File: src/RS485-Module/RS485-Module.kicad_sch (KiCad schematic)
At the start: 29 parts, among them J1 Jumper_NO, J2 Jumper_NO, J3 Jumper_NO, J4 Jumper_NO, J5 Jumper_NO, J6 Jumper_NO, J7 Jumper_NO, J8 Jumper_NO, P1 5015680807, P2 282837-2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

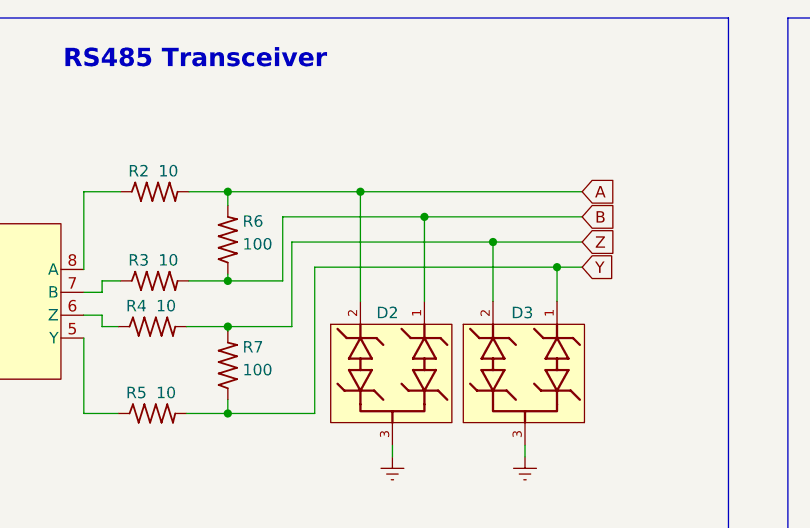
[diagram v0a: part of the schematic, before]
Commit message: placed components in layoyut
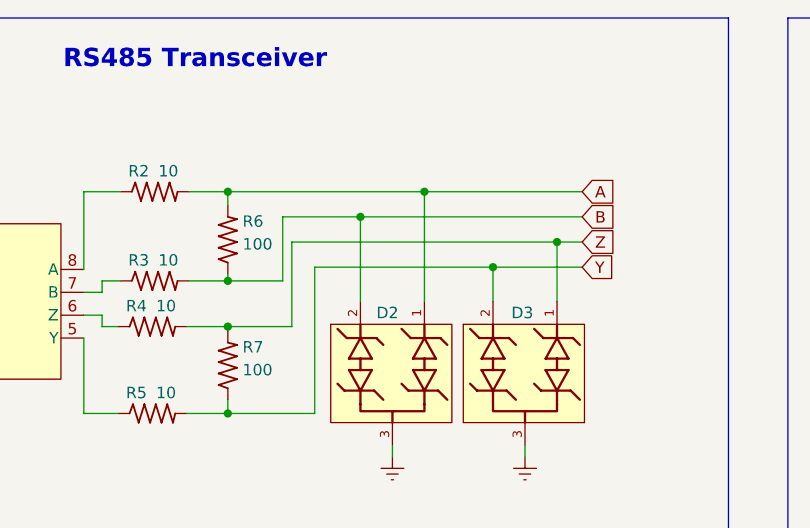
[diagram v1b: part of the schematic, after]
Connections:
- net A: now also D2.1; no longer D2.2
- net B: now also D2.2; no longer D2.1
- net Y: now also D3.2; no longer D3.1
- net Z: now also D3.1; no longer D3.2
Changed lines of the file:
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@@
   (junction (at 166.116 44.958) (diameter 0) (color 0 0 0 0)
   )
-  (junction (at 202.692 53.34) (diameter 0) (color 0 0 0 0)
-  )
   (junction (at 53.594 62.23) (diameter 0) (color 0 0 0 0)
   )
@@
   (junction (at 166.116 59.944) (diameter 0) (color 0 0 0 0)
   )
-  (junction (at 180.848 44.958) (diameter 0) (color 0 0 0 0)
-  )
   (junction (at 108.204 53.34) (diameter 0) (color 0 0 0 0)
   )
+  (junction (at 180.848 47.752) (diameter 0) (color 0 0 0 0)
+  )
   (junction (at 156.972 110.998) (diameter 0) (color 0 0 0 0)
   )
@@
   (junction (at 156.718 122.174) (diameter 0) (color 0 0 0 0)
   )
-  (junction (at 195.58 50.546) (diameter 0) (color 0 0 0 0)
+  (junction (at 187.96 44.958) (diameter 0) (color 0 0 0 0)
+  )
+  (junction (at 195.58 53.34) (diameter 0) (color 0 0 0 0)
   )
   (junction (at 53.594 59.69) (diameter 0) (color 0 0 0 0)
   )
-  (junction (at 187.96 47.752) (diameter 0) (color 0 0 0 0)
+  (junction (at 202.692 50.546) (diameter 0) (color 0 0 0 0)
   )
   (junction (at 166.116 69.596) (diameter 0) (color 0 0 0 0)
@@
     (stroke (width 0) (type default))
   )
+  (wire (pts (xy 202.692 50.546) (xy 202.692 57.15))
+    (stroke (width 0) (type default))
+  )
   (wire (pts (xy 106.68 53.34) (xy 108.204 53.34))
     (stroke (width 0) (type default))
@@
     (stroke (width 0) (type default))
   )
-  (wire (pts (xy 195.58 57.15) (xy 195.58 50.546))
-    (stroke (width 0) (type default))
-  )
   (wire (pts (xy 55.118 44.45) (xy 50.546 44.45))
     (stroke (width 0) (type default))
@@
     (stroke (width 0) (type default))
   )
+  (wire (pts (xy 195.58 53.34) (xy 205.486 53.34))
+    (stroke (width 0) (type default))
+  )
   (wire (pts (xy 141.478 112.522) (xy 145.034 112.522))
     (stroke (width 0) (type default))
@@
     (stroke (width 0) (type default))
   )
-  (wire (pts (xy 195.58 50.546) (xy 205.486 50.546))
-    (stroke (width 0) (type default))
-  )
   (wire (pts (xy 159.512 122.174) (xy 156.718 122.174))
     (stroke (width 0) (type default))
@@
     (stroke (width 0) (type default))
   )
-  (wire (pts (xy 175.768 53.34) (xy 202.692 53.34))
+  (wire (pts (xy 175.768 53.34) (xy 195.58 53.34))
     (stroke (width 0) (type default))
   )
@@
     (stroke (width 0) (type default))
   )
-  (wire (pts (xy 180.848 44.958) (xy 205.486 44.958))
-    (stroke (width 0) (type default))
-  )
   (wire (pts (xy 141.478 143.002) (xy 144.018 143.002))
     (stroke (width 0) (type default))
@@
     (stroke (width 0) (type default))
   )
-  (wire (pts (xy 166.116 44.958) (xy 180.848 44.958))
+  (wire (pts (xy 166.116 44.958) (xy 187.96 44.958))
     (stroke (width 0) (type default))
   )
@@
     (stroke (width 0) (type default))
   )
+  (wire (pts (xy 180.848 47.752) (xy 180.848 57.15))
+    (stroke (width 0) (type default))
+  )
   (wire (pts (xy 166.116 54.864) (xy 172.212 54.864))
     (stroke (width 0) (type default))
@@
     (stroke (width 0) (type default))
   )
-  (wire (pts (xy 202.692 53.34) (xy 205.486 53.34))
+  (wire (pts (xy 202.692 50.546) (xy 205.486 50.546))
     (stroke (width 0) (type default))
   )
@@
     (stroke (width 0) (type default))
   )
-  (wire (pts (xy 173.228 50.546) (xy 195.58 50.546))
+  (wire (pts (xy 173.228 50.546) (xy 202.692 50.546))
     (stroke (width 0) (type default))
   )
@@
     (stroke (width 0) (type default))
   )
-  (wire (pts (xy 180.848 44.958) (xy 180.848 57.15))
-    (stroke (width 0) (type default))
-  )
   (wire (pts (xy 141.224 123.698) (xy 144.78 123.698))
     (stroke (width 0) (type default))
@@
     (stroke (width 0) (type default))
   )
-  (wire (pts (xy 202.692 57.15) (xy 202.692 53.34))
-    (stroke (width 0) (type default))
-  )
   (wire (pts (xy 199.136 73.152) (xy 199.136 74.422))
     (stroke (width 0) (type default))
   )
+  (wire (pts (xy 187.96 44.958) (xy 205.486 44.958))
+    (stroke (width 0) (type default))
+  )
   (wire (pts (xy 122.428 55.88) (xy 124.714 55.88))
     (stroke (width 0) (type default))
@@
     (stroke (width 0) (type default))
   )
-  (wire (pts (xy 187.96 47.752) (xy 187.96 57.15))
+  (wire (pts (xy 180.848 47.752) (xy 205.486 47.752))
+    (stroke (width 0) (type default))
+  )
+  (wire (pts (xy 187.96 57.15) (xy 187.96 44.958))
     (stroke (width 0) (type default))
   )
@@
     (stroke (width 0) (type default))
   )
+  (wire (pts (xy 195.58 53.34) (xy 195.58 57.15))
+    (stroke (width 0) (type default))
+  )
   (wire (pts (xy 50.546 57.15) (xy 53.594 57.15))
     (stroke (width 0) (type default))
   )
-  (wire (pts (xy 187.96 47.752) (xy 205.486 47.752))
-    (stroke (width 0) (type default))
-  )
   (wire (pts (xy 156.972 109.474) (xy 156.972 110.998))
     (stroke (width 0) (type default))
@@
     (stroke (width 0) (type default))
   )
-  (wire (pts (xy 172.212 47.752) (xy 187.96 47.752))
-    (stroke (width 0) (type default))
-  )
+  (wire (pts (xy 172.212 47.752) (xy 180.848 47.752))
+    (stroke (width 0) (type default))
+  )
